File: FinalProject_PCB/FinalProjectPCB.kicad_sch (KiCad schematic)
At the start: 0 parts

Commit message: added Devboard to kicad
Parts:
- added U1: ESP32-S2-DevKitC-1, PCM_Espressif:ESP32-S2-DevKitC-1, symbol PCM_Espressif:ESP32-S2-DevKitC-1
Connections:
- new net 5V: U1.21 (5V)
- new net GND: U1.22 (GND)
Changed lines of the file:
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@@
 	(generator_version "9.0")
 	(paper "A4")
+	(global_label "GND"
+		(shape input)
+		(at 81.28 109.22 180)
+		(fields_autoplaced yes)
+		(effects
+			(font
+				(size 1.27 1.27)
+			)
+			(justify right)
+		)
+		(property "Intersheetrefs" "${INTERSHEET_REFS}"
+			(at 74.4243 109.22 0)
+			(effects
+				(font
+					(size 1.27 1.27)
+				)
+				(justify right)
+				(hide yes)
+			)
+		)
+	)
+	(global_label "5V"
+		(shape input)
+		(at 81.28 106.68 180)
+		(fields_autoplaced yes)
+		(effects
+			(font
+				(size 1.27 1.27)
+			)
+			(justify right)
+		)
+		(property "Intersheetrefs" "${INTERSHEET_REFS}"
+			(at 75.9967 106.68 0)
+			(effects
+				(font
+					(size 1.27 1.27)
+				)
+				(justify right)
+				(hide yes)
+			)
+		)
+	)
+	(symbol
+		(lib_id "PCM_Espressif:ESP32-S2-DevKitC-1")
+		(at 106.68 81.28 0)
+		(unit 1)
+		(exclude_from_sim no)
+		(in_bom yes)
+		(on_board yes)
+		(dnp no)
+		(fields_autoplaced yes)
+		(property "Reference" "U1"
+			(at 106.68 48.26 0)
+			(effects
+				(font
+					(size 1.27 1.27)
+				)
+			)
+		)
+		(property "Value" "ESP32-S2-DevKitC-1"
+			(at 106.68 50.8 0)
+			(effects
+				(font
+					(size 1.27 1.27)
+				)
+			)
+		)
+		(property "Footprint" "PCM_Espressif:ESP32-S2-DevKitC-1"
+			(at 106.68 114.3 0)
+			(effects
+				(font
+					(size 1.27 1.27)
+				)
+				(hide yes)
+			)
+		)
+		(property "Datasheet" "https://docs.espressif.com/projects/esp-idf/en/latest/esp32s2/hw-reference/esp32s2/user-guide-s2-devkitc-1.html"
+			(at 118.11 116.84 0)
+			(effects
+				(font
+					(size 1.27 1.27)
+				)
+				(hide yes)
+			)
+		)
+		(property "Description" "ESP32-S2-DevKitC-1"
+			(at 106.68 81.28 0)
+			(effects
+				(font
+					(size 1.27 1.27)
+				)
+				(hide yes)
+			)
+		)
+		(pin "5"
+		)
+		(pin "9"
+		)
+		(pin "2"
+		)
+		(pin "7"
+		)
+		(pin "23"
+		)
+		(pin "13"
+		)
+		(pin "15"
+		)
+		(pin "16"
+		)
+		(pin "17"
+		)
+		(pin "25"
+		)
+		(pin "38"
+		)
+		(pin "37"
+		)
+		(pin "29"
+		)
+		(pin "28"
+		)
+		(pin "27"
+		)
+		(pin "26"
+		)
+		(pin "10"
+		)
+		(pin "11"
+		)
+		(pin "12"
+		)
+		(pin "24"
+		)
+		(pin "18"
+		)
+		(pin "20"
+		)
+		(pin "8"
+		)
+		(pin "36"
+		)
+		(pin "35"
+		)
+		(pin "34"
+		)
+		(pin "33"
+		)
+		(pin "21"
+		)
+		(pin "22"
+		)
+		(pin "32"
+		)
+		(pin "31"
+		)
+		(pin "30"
+		)
+		(pin "19"
+		)
+		(pin "3"
+		)
+		(pin "6"
+		)
+		(pin "1"
+		)
+		(pin "39"
+		)
+		(pin "43"
+		)
+		(pin "4"
+		)
+		(pin "40"
+		)
+		(pin "41"
+		)
+		(pin "42"
+		)
+		(pin "14"
+		)
+		(pin "44"
+		)
+		(instances
+			(project ""
+				(path "/779a3c99-a5a8-445d-8f38-e1d85c7e87cc"
+					(reference "U1")
+					(unit 1)
+				)
+			)
+		)
+	)
 	(sheet_instances
 		(path "/"

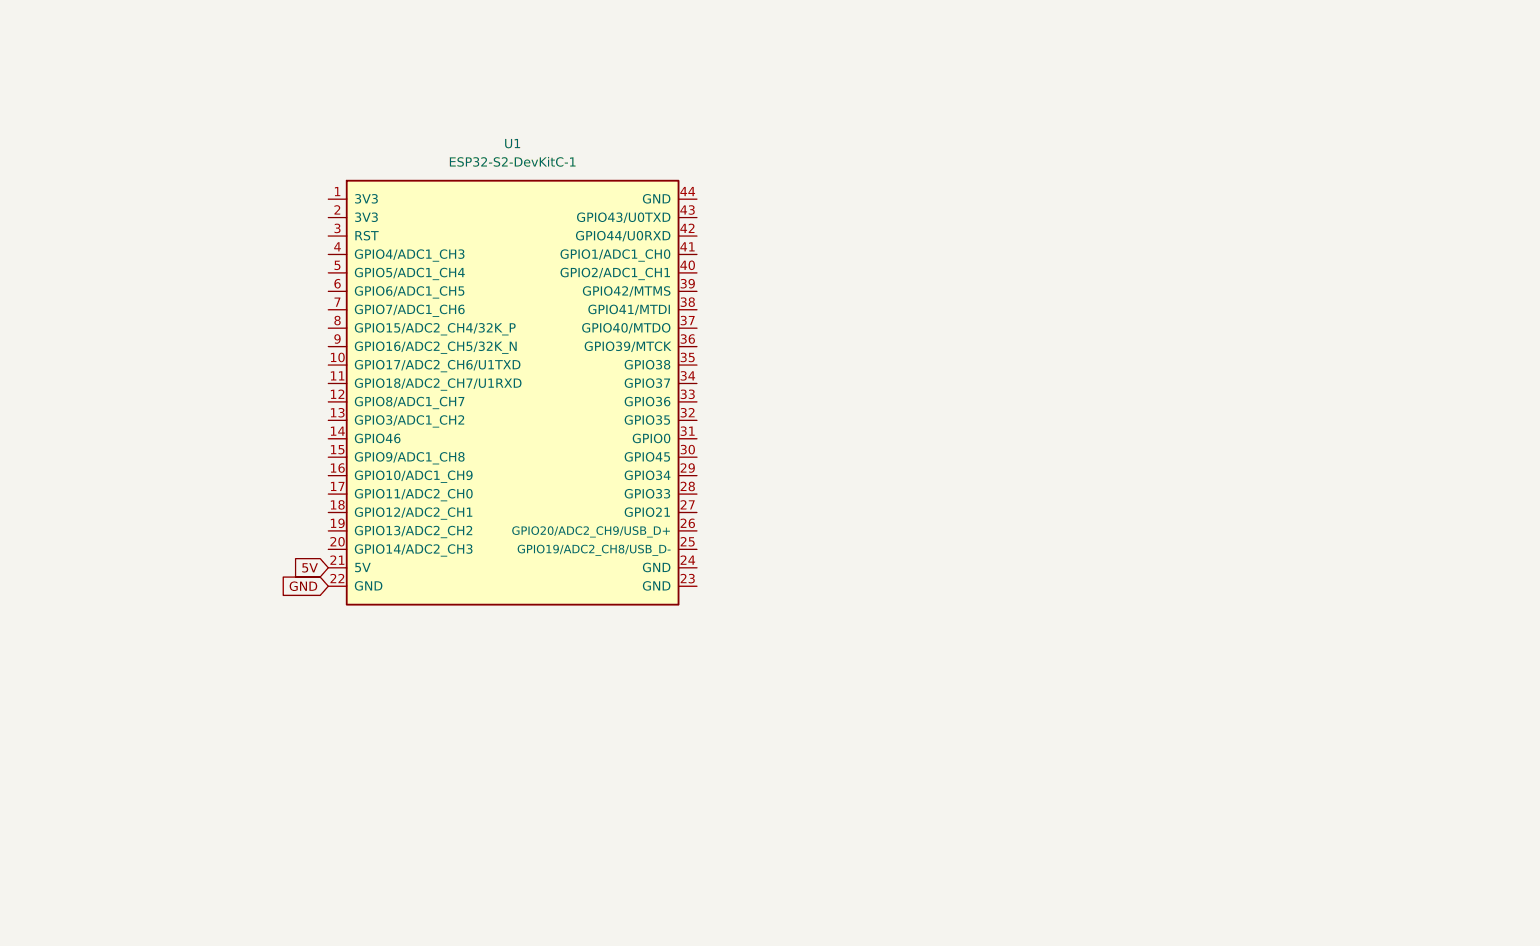
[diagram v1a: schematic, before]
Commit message: added components
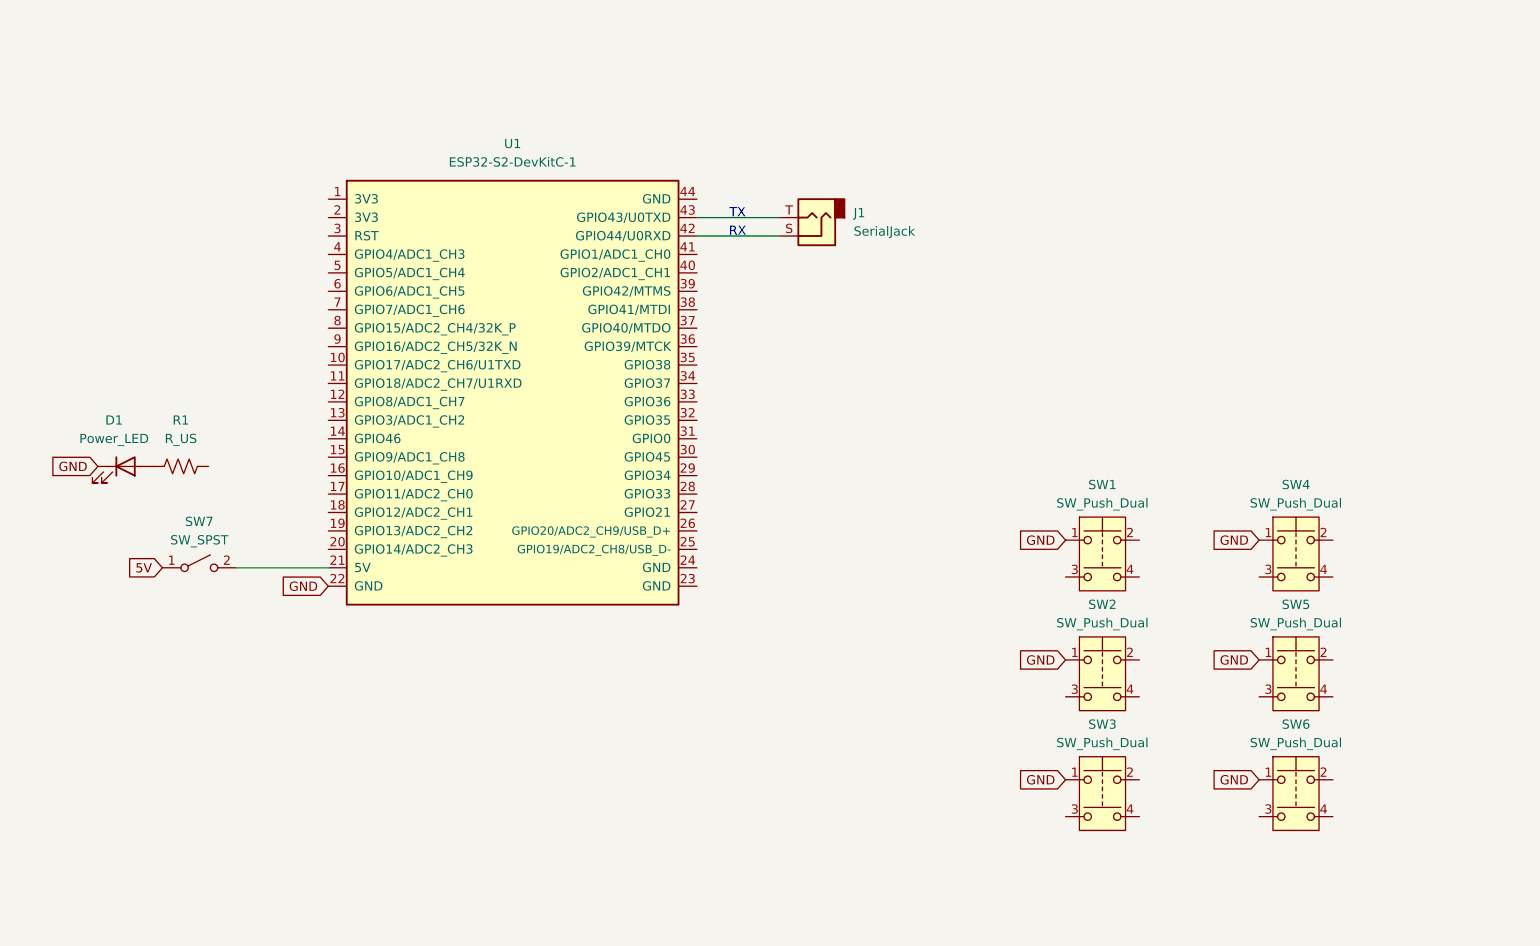
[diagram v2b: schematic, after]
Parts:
- added D1: Power_LED, symbol Device:LED
- added J1: SerialJack, symbol Connector_Audio:AudioJack2
- added R1: R_US, symbol Device:R_US
- added SW1, SW2, SW3, SW4, SW5, SW6: SW_Push_Dual, symbol Switch:SW_Push_Dual
- added SW7: SW_SPST, symbol Switch:SW_SPST
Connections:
- net 5V: now also SW7.1 (A); no longer U1.21 (5V)
- net GND: now also D1.1 (K), SW1.1, SW2.1, SW3.1, SW4.1, SW5.1, SW6.1
- net at U1.42 (GPIO44/U0RXD): now also J1.S
- net at U1.43 (GPIO43/U0TXD): now also J1.T
- new net: SW7.2 (B), U1.21 (5V)
- new net: D1.2 (A), R1.1
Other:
- note added: "RX"
- note added: "TX"

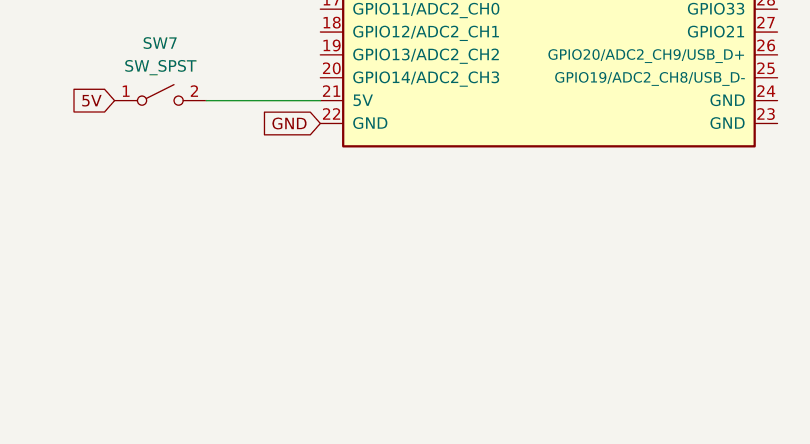
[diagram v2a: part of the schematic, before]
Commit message: added Piezo
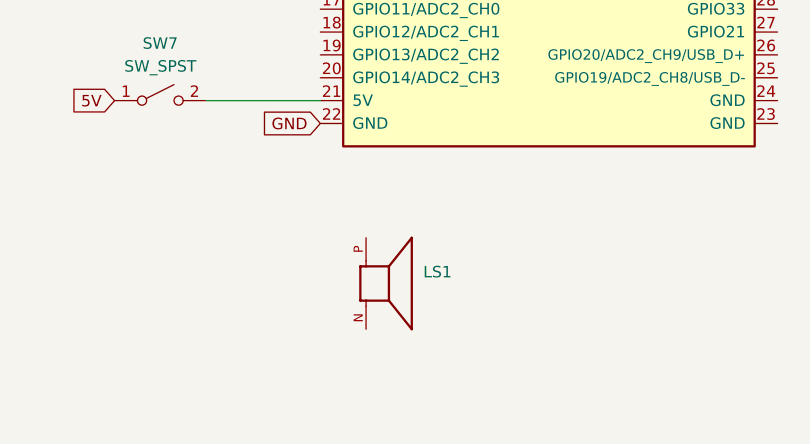
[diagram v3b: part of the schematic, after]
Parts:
- added LS1: ~, Piezo, symbol Piezo_AT-1224-TWT-5V-2-R:AT-1224-TWT-5V-2-R
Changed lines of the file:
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@@
+	)
+	(symbol
+		(lib_id "Piezo_AT-1224-TWT-5V-2-R:AT-1224-TWT-5V-2-R")
+		(at 88.9 127 0)
+		(unit 1)
+		(exclude_from_sim no)
+		(in_bom yes)
+		(on_board yes)
+		(dnp no)
+		(fields_autoplaced yes)
+		(property "Reference" "LS1"
+			(at 92.71 125.7299 0)
+			(effects
+				(font
+					(size 1.27 1.27)
+				)
+				(justify left)
+			)
+		)
+		(property "Value" "~"
+			(at 92.71 128.2699 0)
+			(effects
+				(font
+					(size 1.27 1.27)
+				)
+				(justify left)
+			)
+		)
+		(property "Footprint" "Piezo"
+			(at 94.234 127 0)
+			(effects
+				(font
+					(size 1.27 1.27)
+				)
+				(justify bottom)
+				(hide yes)
+			)
+		)
+		(property "Datasheet" ""
+			(at 88.9 127 0)
+			(effects
+				(font
+					(size 1.27 1.27)
+				)
+				(hide yes)
+			)
+		)
+		(property "Description" ""
+			(at 88.9 127 0)
+			(effects
+				(font
+					(size 1.27 1.27)
+				)
+				(hide yes)
+			)
+		)
+		(property "PARTREV" ""
+			(at 88.392 113.03 0)
+			(effects
+				(font
+					(size 1.27 1.27)
+				)
+				(justify bottom)
+				(hide yes)
+			)
+		)
+		(property "STANDARD" ""
+			(at 75.438 141.478 0)
+			(effects
+				(font
+					(size 1.27 1.27)
+				)
+				(justify bottom)
+				(hide yes)
+			)
+		)
+		(property "MAXIMUM_PACKAGE_HEIGHT" ""
+			(at 78.232 128.524 0)
+			(effects
+				(font
+					(size 1.27 1.27)
+				)
+				(justify bottom)
+				(hide yes)
+			)
+		)
+		(property "MANUFACTURER" ""
+			(at 77.47 132.842 0)
+			(effects
+				(font
+					(size 1.27 1.27)
+				)
+				(justify bottom)
+				(hide yes)
+			)
+		)
+		(pin "P"
+		)
+		(pin "N"
+		)
+		(instances
+			(project ""
+				(path "/779a3c99-a5a8-445d-8f38-e1d85c7e87cc"
+					(reference "LS1")
+					(unit 1)
+				)
+			)
+		)
 	)
 	(symbol

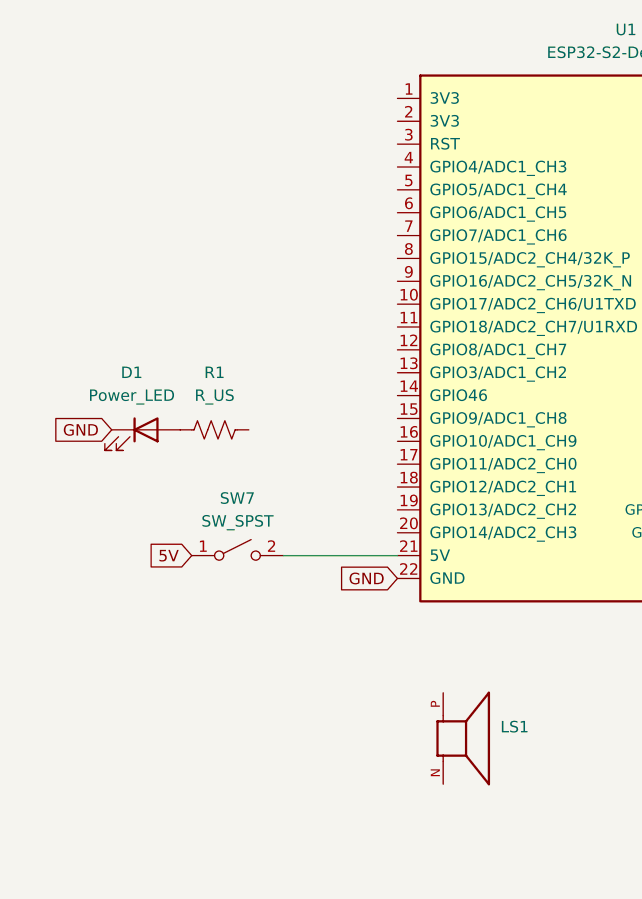
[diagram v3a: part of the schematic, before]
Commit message: added volume slider
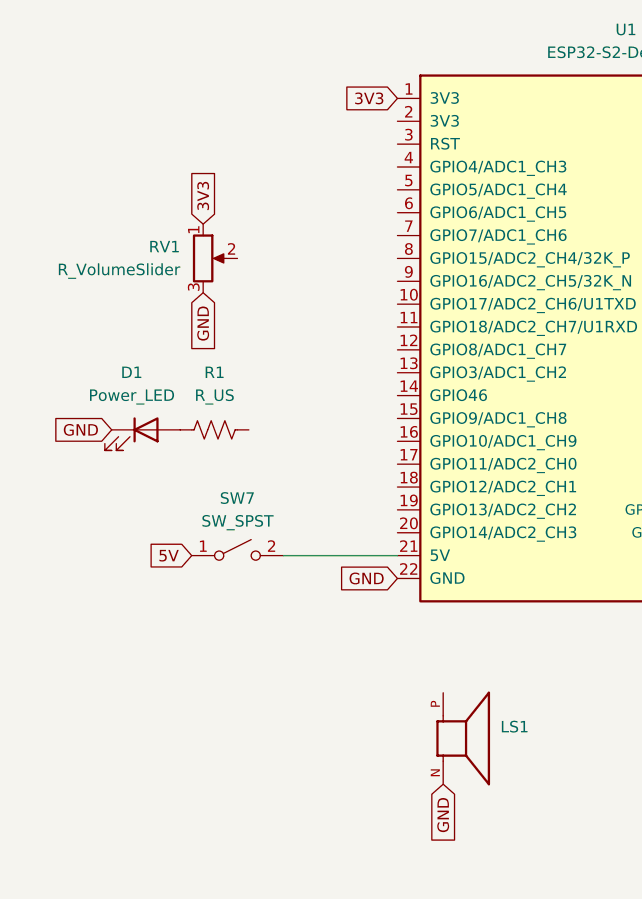
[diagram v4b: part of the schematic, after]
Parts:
- added RV1: R_VolumeSlider, symbol Device:R_Potentiometer
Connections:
- net GND: now also LS1.N, RV1.3
- net 3V3: now reaches U1.1 (3V3)
- net 3V3: now also RV1.1
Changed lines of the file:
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@@
+		)
+	)
+	(global_label "3V3"
+		(shape input)
+		(at 59.69 69.85 90)
+		(fields_autoplaced yes)
+		(effects
+			(font
+				(size 1.27 1.27)
+			)
+			(justify left)
+		)
+		(property "Intersheetrefs" "${INTERSHEET_REFS}"
+			(at 59.69 63.3572 90)
+			(effects
+				(font
+					(size 1.27 1.27)
+				)
+				(justify left)
+				(hide yes)
+			)
 		)
 	)
@@
 		)
 	)
+	(global_label "3V3"
+		(shape input)
+		(at 81.28 55.88 180)
+		(fields_autoplaced yes)
+		(effects
+			(font
+				(size 1.27 1.27)
+			)
+			(justify right)
+		)
+		(property "Intersheetrefs" "${INTERSHEET_REFS}"
+			(at 74.7872 55.88 0)
+			(effects
+				(font
+					(size 1.27 1.27)
+				)
+				(justify right)
+				(hide yes)
+			)
+		)
+	)
 	(global_label "GND"
 		(shape input)
+		(at 59.69 77.47 270)
+		(fields_autoplaced yes)
+		(effects
+			(font
+				(size 1.27 1.27)
+			)
+			(justify right)
+		)
+		(property "Intersheetrefs" "${INTERSHEET_REFS}"
+			(at 59.69 84.3257 90)
+			(effects
+				(font
+					(size 1.27 1.27)
+				)
+				(justify right)
+				(hide yes)
+			)
+		)
+	)
+	(global_label "GND"
+		(shape input)
 		(at 182.88 135.89 180)
 		(fields_autoplaced yes)
@@
 		(property "Intersheetrefs" "${INTERSHEET_REFS}"
 			(at 176.0243 102.87 0)
+			(effects
+				(font
+					(size 1.27 1.27)
+				)
+				(justify right)
+				(hide yes)
+			)
+		)
+	)
+	(global_label "GND"
+		(shape input)
+		(at 86.36 132.08 270)
+		(fields_autoplaced yes)
+		(effects
+			(font
+				(size 1.27 1.27)
+			)
+			(justify right)
+		)
+		(property "Intersheetrefs" "${INTERSHEET_REFS}"
+			(at 86.36 138.9357 90)
 			(effects
 				(font
@@
 					(unit 1)
 				)
+			)
+		)
+	)
+	(symbol
+		(lib_id "Device:R_Potentiometer")
+		(at 59.69 73.66 0)
+		(unit 1)
+		(exclude_from_sim no)
+		(in_bom yes)
+		(on_board yes)
+		(dnp no)
+		(fields_autoplaced yes)
+		(property "Reference" "RV1"
+			(at 57.15 72.3899 0)
+			(effects
+				(font
+					(size 1.27 1.27)
+				)
+				(justify right)
+			)
+		)
+		(property "Value" "R_VolumeSlider"
+			(at 57.15 74.9299 0)
+			(effects
+				(font
+					(size 1.27 1.27)
+				)
+				(justify right)
+			)
+		)
+		(property "Footprint" ""
+			(at 59.69 73.66 0)
+			(effects
+				(font
+					(size 1.27 1.27)
+				)
+				(hide yes)
+			)
+		)
+		(property "Datasheet" "~"
+			(at 59.69 73.66 0)
+			(effects
+				(font
+					(size 1.27 1.27)
+				)
+				(hide yes)
+			)
+		)
+		(property "Description" "Potentiometer"
+			(at 59.69 73.66 0)
+			(effects
+				(font
+					(size 1.27 1.27)
+				)
+				(hide yes)
+			)
+		)
+		(pin "2"
+		)
+		(pin "1"
+		)
+		(pin "3"
+		)
+		(instances
+			(project ""
+				(path "/779a3c99-a5a8-445d-8f38-e1d85c7e87cc"
+					(reference "RV1")
+					(unit 1)
+				)
